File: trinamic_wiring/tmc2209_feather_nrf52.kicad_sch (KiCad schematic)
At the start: 4 parts, among them M1 Stepper_Motor_QSH2818-32-07-0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

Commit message: Update tmc2209 nrf52
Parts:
- gave numbers to parts that had none: 1
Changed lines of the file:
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@@
   (symbol (lib_id "Janelia:FEATHERWING_nRF52_PIN_RECEPTACLES") (at 74.93 100.33 0) (unit 1)
     (in_bom yes) (on_board yes)
-    (property "Reference" "FEATHER?" (id 0) (at 74.93 74.93 0))
+    (property "Reference" "FEATHER1" (id 0) (at 74.93 74.93 0))
     (property "Value" "FEATHER_nRF52" (id 1) (at 74.93 127 0))
     (property "Footprint" "Janelia:FEATHERWING_PIN_RECEPTACLES" (id 2) (at 74.93 66.04 0)

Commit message: Update version
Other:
- company: (none) -> Janelia Research Campus
- title: TMC2209 MEGA2560 -> Trinamic Wiring

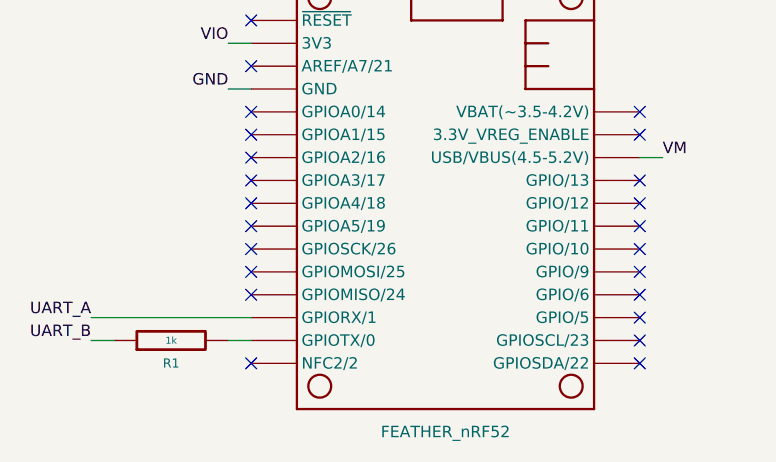
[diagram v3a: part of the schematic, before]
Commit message: miso -> cipo, mosi -> copi
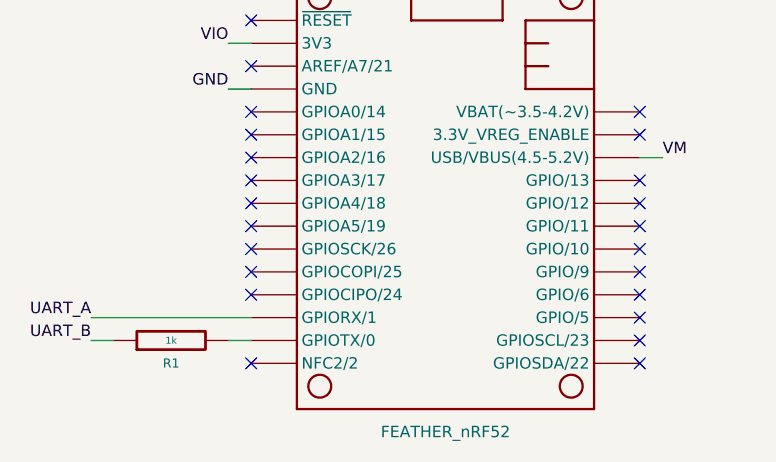
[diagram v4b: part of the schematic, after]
